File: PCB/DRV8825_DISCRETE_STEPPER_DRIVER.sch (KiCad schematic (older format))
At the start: 12 parts, among them U2 DRV8825PWPR

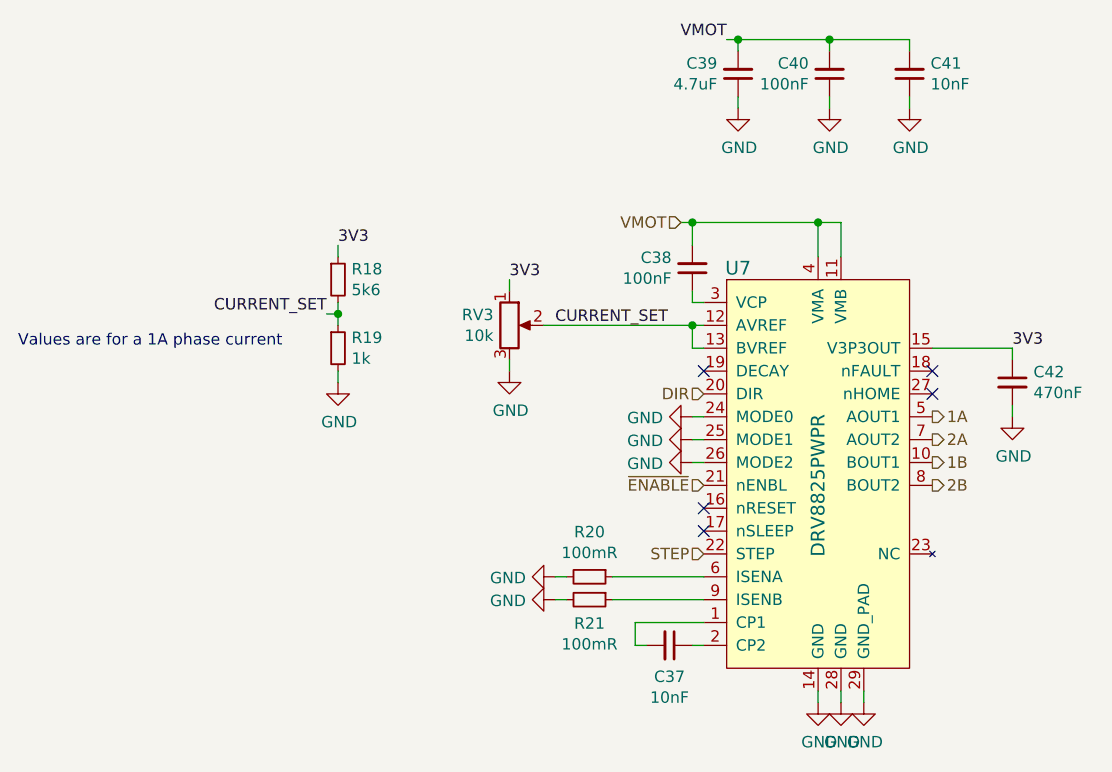
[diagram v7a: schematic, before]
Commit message: Added Dielectric and voltage rating to all capacitors
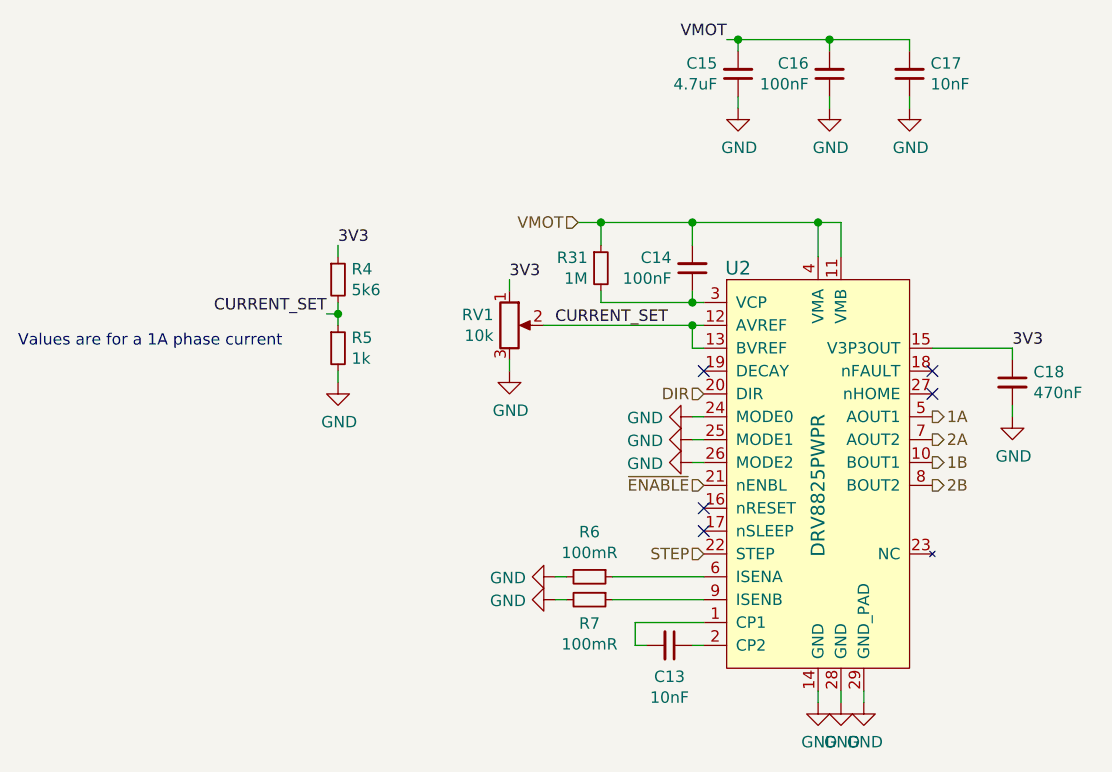
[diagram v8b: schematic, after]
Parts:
- added R31: 1M, symbol Device:R_Small
- C13: Dielectric (none) -> X7R; Voltage Rating (none) -> 50V
- C14: Dielectric (none) -> X7R; Voltage Rating (none) -> 16V
- C15: Dielectric (none) -> Aluminium Film; Impedance (none) -> General Purpose; Lifetime @ Temperature (none) -> 1000hr @ 85degC
- C16, C17: Dielectric (none) -> X7R
- C18: Dielectric (none) -> X7R; Voltage Rating (none) -> 6.3V
- R6, R7: Power Rating (none) -> 1W
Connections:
- net VMOT: now also R31.1
- net at C14.1, U2.3 (VCP): now also R31.2
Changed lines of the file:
@@
 $Descr A4 11693 8268
 encoding utf-8
-Sheet 4 20
+Sheet 14 20
 Title ""
 Date ""
@@
 AR Path="/5E8A6686/5E8D27A6/5E8D3351" Ref="U2"  Part="1"
 AR Path="/5E8813FF/5E8D27A6/5E8D3351" Ref="U7"  Part="1"
-F 0 "U7" H 5300 4500 60  0000 C CNN
+F 0 "U2" H 5300 4500 60  0000 C CNN
 F 1 "DRV8825PWPR" V 5650 3550 60  0000 C CNN
 F 2 "digikey-footprints:TSSOP-28-1EP_W4.40mm" H 5750 4050 60  0001 L CNN
@@
 AR Path="/5E8A6686/5E8D27A6/5E8D575F" Ref="C13"  Part="1"
 AR Path="/5E8813FF/5E8D27A6/5E8D575F" Ref="C37"  Part="1"
-F 0 "C37" V 5137 4850 50  0000 C CNN
+F 0 "C13" V 5137 4850 50  0000 C CNN
 F 1 "10nF" V 5228 4850 50  0000 C CNN
 F 2 "" H 5000 4850 50  0001 C CNN
 F 3 "" H 5000 4850 50  0001 C CNN
+F 4 "X7R" H 5000 4850 50  0001 C CNN "Dielectric"
+F 5 "50V" H 5000 4850 50  0001 C CNN "Voltage Rating"
 	1    5000 4850
 	0    1    1    0
@@
 AR Path="/5E8A6686/5E8D27A6/5E8D7A25" Ref="R6"  Part="1"
 AR Path="/5E8813FF/5E8D27A6/5E8D7A25" Ref="R20"  Part="1"
-F 0 "R20" V 4454 4550 50  0000 C CNN
+F 0 "R6" V 4454 4550 50  0000 C CNN
 F 1 "100mR" V 4545 4550 50  0000 C CNN
 F 2 "" H 4650 4550 50  0001 C CNN
 F 3 "" H 4650 4550 50  0001 C CNN
+F 4 "1W" H 4650 4550 50  0001 C CNN "Power Rating"
 	1    4650 4550
 	0    1    1    0
@@
 AR Path="/5E8A6686/5E8D27A6/5E8D7F7E" Ref="R7"  Part="1"
 AR Path="/5E8813FF/5E8D27A6/5E8D7F7E" Ref="R21"  Part="1"
-F 0 "R21" V 4754 4650 50  0000 C CNN
+F 0 "R7" V 4754 4650 50  0000 C CNN
 F 1 "100mR" V 4845 4650 50  0000 C CNN
 F 2 "" H 4650 4650 50  0001 C CNN
 F 3 "" H 4650 4650 50  0001 C CNN
+F 4 "1W" H 4650 4650 50  0001 C CNN "Power Rating"
 	1    4650 4650
 	0    1    1    0
@@
 AR Path="/5E8A6686/5E8D27A6/5E8DA337" Ref="C14"  Part="1"
 AR Path="/5E8813FF/5E8D27A6/5E8DA337" Ref="C38"  Part="1"
-F 0 "C38" H 5191 3154 50  0000 L CNN
+F 0 "C14" H 5191 3154 50  0000 L CNN
 F 1 "100nF" H 5191 3245 50  0000 L CNN
 F 2 "" H 5100 3200 50  0001 C CNN
 F 3 "" H 5100 3200 50  0001 C CNN
+F 4 "X7R" H 5100 3200 50  0001 C CNN "Dielectric"
+F 5 "16V" H 5100 3200 50  0001 C CNN "Voltage Rating"
 	1    5100 3200
 	-1   0    0    1
@@
 Wire Wire Line
 	5100 3350 5150 3350
-Text HLabel 5050 3000 0    50   Input ~ 0
+Text HLabel 4600 3000 0    50   Input ~ 0
 VMOT
 Wire Wire Line
@@
 	5650 3150 5650 3000
 Wire Wire Line
-	5050 3000 5100 3000
+	4600 3000 4700 3000
 Connection ~ 5650 3000
 Wire Wire Line
@@
 AR Path="/5E8A6686/5E8D27A6/5E8DF1FC" Ref="RV1"  Part="1"
 AR Path="/5E8813FF/5E8D27A6/5E8DF1FC" Ref="RV3"  Part="1"
-F 0 "RV3" H 4230 3496 50  0000 R CNN
+F 0 "RV1" H 4230 3496 50  0000 R CNN
 F 1 "10k" H 4230 3405 50  0000 R CNN
 F 2 "" H 4300 3450 50  0001 C CNN
@@
 AR Path="/5E8A6686/5E8D27A6/5E8E181B" Ref="C18"  Part="1"
 AR Path="/5E8813FF/5E8D27A6/5E8E181B" Ref="C42"  Part="1"
-F 0 "C42" H 6592 3746 50  0000 L CNN
+F 0 "C18" H 6592 3746 50  0000 L CNN
 F 1 "470nF" H 6592 3655 50  0000 L CNN
 F 2 "" H 6500 3700 50  0001 C CNN
 F 3 "" H 6500 3700 50  0001 C CNN
+F 4 "X7R" H 6500 3700 50  0001 C CNN "Dielectric"
+F 5 "6.3V" H 6500 3700 50  0001 C CNN "Voltage Rating"
 	1    6500 3700
 	1    0    0    -1
@@
 AR Path="/5E8A6686/5E8D27A6/5E8E9760" Ref="C15"  Part="1"
 AR Path="/5E8813FF/5E8D27A6/5E8E9760" Ref="C39"  Part="1"
-F 0 "C39" H 5391 2304 50  0000 L CNN
+F 0 "C15" H 5391 2304 50  0000 L CNN
 F 1 "4.7uF" H 5391 2395 50  0000 L CNN
 F 2 "" H 5300 2350 50  0001 C CNN
 F 3 "" H 5300 2350 50  0001 C CNN
 F 4 "50V" H 5300 2350 50  0001 C CNN "Voltage Rating"
+F 5 "Aluminium Film" H 5300 2350 50  0001 C CNN "Dielectric"
+F 6 "General Purpose" H 5300 2350 50  0001 C CNN "Impedance"
+F 7 "1000hr @ 85degC" H 5300 2350 50  0001 C CNN "Lifetime @ Temperature"
 	1    5300 2350
 	-1   0    0    1
@@
 AR Path="/5E8A6686/5E8D27A6/5E8E999E" Ref="C16"  Part="1"
 AR Path="/5E8813FF/5E8D27A6/5E8E999E" Ref="C40"  Part="1"
-F 0 "C40" H 5791 2304 50  0000 L CNN
+F 0 "C16" H 5791 2304 50  0000 L CNN
 F 1 "100nF" H 5791 2395 50  0000 L CNN
 F 2 "" H 5700 2350 50  0001 C CNN
 F 3 "" H 5700 2350 50  0001 C CNN
 F 4 "50V" H 5700 2350 50  0001 C CNN "Voltage Rating"
+F 5 "X7R" H 5700 2350 50  0001 C CNN "Dielectric"
 	1    5700 2350
 	-1   0    0    1
@@
 AR Path="/5E8A6686/5E8D27A6/5E8E9DB5" Ref="C17"  Part="1"
 AR Path="/5E8813FF/5E8D27A6/5E8E9DB5" Ref="C41"  Part="1"
-F 0 "C41" H 5958 2304 50  0000 R CNN
+F 0 "C17" H 5958 2304 50  0000 R CNN
 F 1 "10nF" H 5958 2395 50  0000 R CNN
 F 2 "" H 6050 2350 50  0001 C CNN
 F 3 "" H 6050 2350 50  0001 C CNN
 F 4 "50V" H 6050 2350 50  0001 C CNN "Voltage Rating"
+F 5 "X7R" H 6050 2350 50  0001 C CNN "Dielectric"
 	1    6050 2350
 	-1   0    0    1
@@
 AR Path="/5E8A6686/5E8D27A6/5E8B797B" Ref="R4"  Part="1"
 AR Path="/5E8813FF/5E8D27A6/5E8B797B" Ref="R18"  Part="1"
-F 0 "R18" H 3609 3296 50  0000 L CNN
+F 0 "R4" H 3609 3296 50  0000 L CNN
 F 1 "5k6" H 3609 3205 50  0000 L CNN
 F 2 "" H 3550 3250 50  0001 C CNN
@@
 AR Path="/5E8A6686/5E8D27A6/5E8B7AF6" Ref="R5"  Part="1"
 AR Path="/5E8813FF/5E8D27A6/5E8B7AF6" Ref="R19"  Part="1"
-F 0 "R19" H 3609 3596 50  0000 L CNN
+F 0 "R5" H 3609 3596 50  0000 L CNN
 F 1 "1k" H 3609 3505 50  0000 L CNN
 F 2 "" H 3550 3550 50  0001 C CNN
@@
 Text Notes 2150 3550 0    50   ~ 0
 Values are for a 1A phase current
+$Comp
+L Device:R_Small R31
+U 1 1 5E8D6554
+P 4700 3200
+AR Path="/5E8A6686/5E8D27A6/5E8D6554" Ref="R31"  Part="1"
+AR Path="/5E8813FF/5E8D27A6/5E8D6554" Ref="R32"  Part="1"
+F 0 "R31" H 4642 3246 50  0000 R CNN
+F 1 "1M" H 4642 3155 50  0000 R CNN
+F 2 "" H 4700 3200 50  0001 C CNN
+F 3 "" H 4700 3200 50  0001 C CNN
+	1    4700 3200
+	1    0    0    -1
+$EndComp
+Wire Wire Line
+	4700 3300 4700 3350
+Wire Wire Line
+	4700 3350 5100 3350
+Connection ~ 5100 3350
+Wire Wire Line
+	4700 3100 4700 3000
+Connection ~ 4700 3000
+Wire Wire Line
+	4700 3000 5100 3000
 $EndSCHEMATC
